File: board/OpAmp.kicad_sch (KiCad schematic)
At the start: 15 parts, among them U3 Opamp_Dual, U8 Opamp_Dual

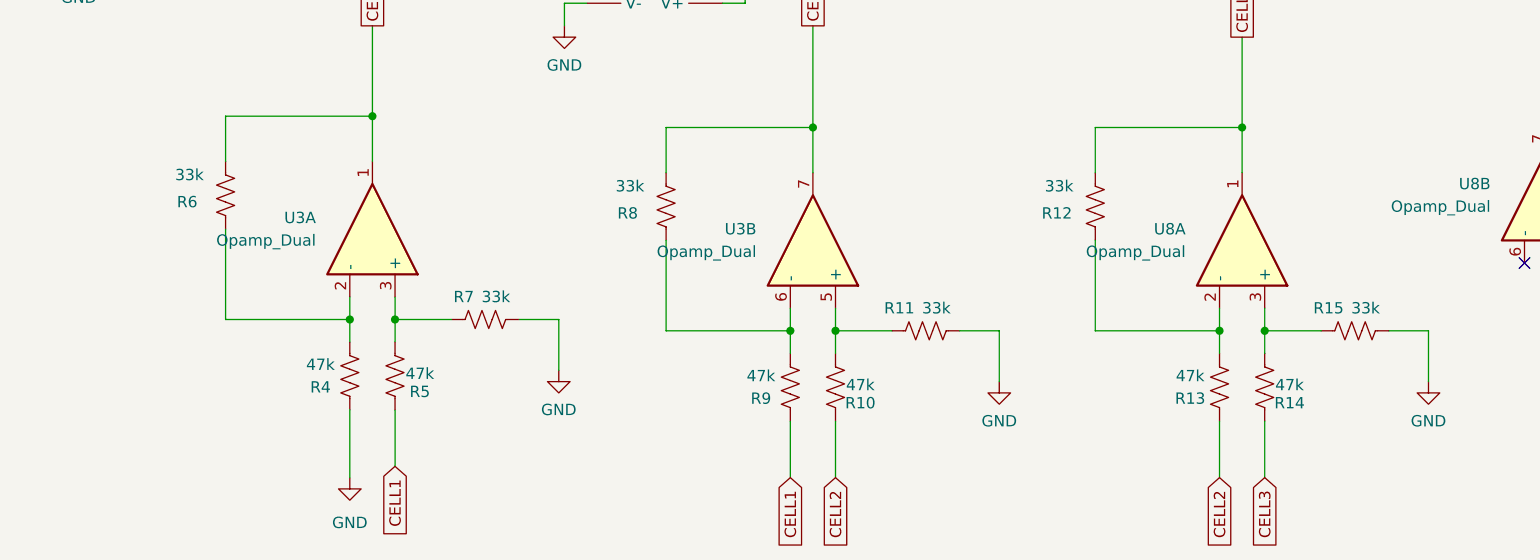
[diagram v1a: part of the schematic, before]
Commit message: Add Corrected Op-Amp Resistor Values
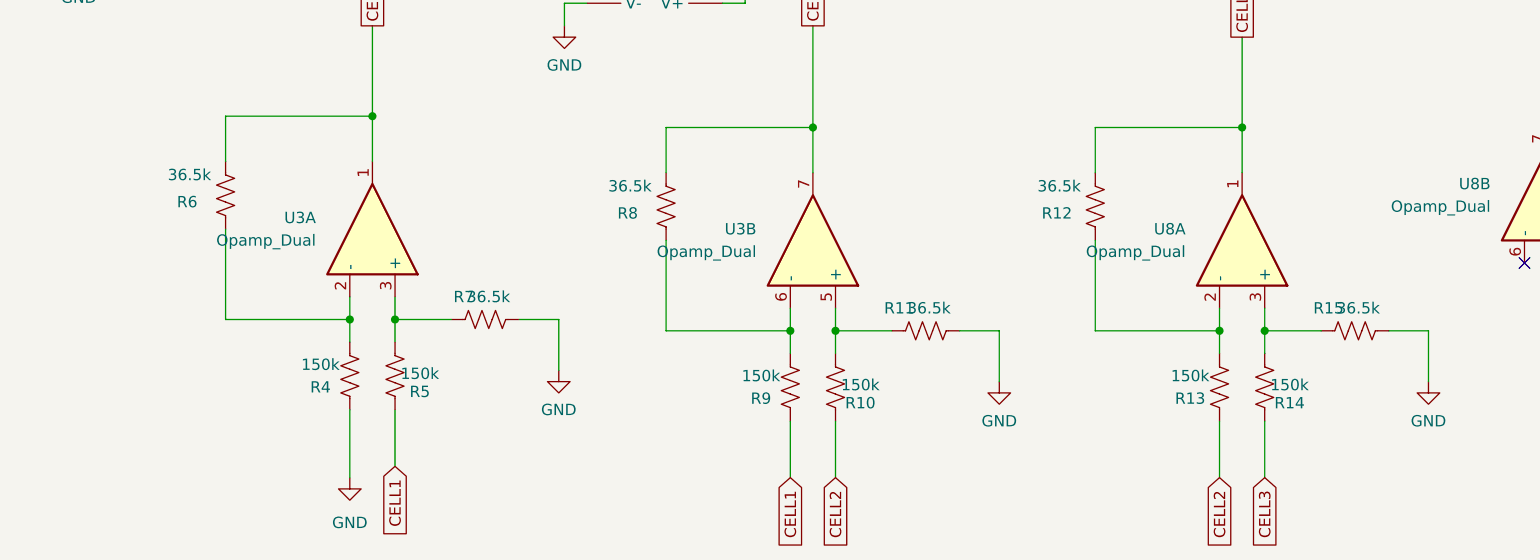
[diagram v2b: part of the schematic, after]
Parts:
- R10, R13, R14, R4, R5, R9: value 47k -> 150k
- R11, R12, R15, R6, R7, R8: value 33k -> 36.5k
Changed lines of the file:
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@@
 			)
 		)
-		(property "Value" "47k"
+		(property "Value" "150k"
 			(at 169.418 138.43 0)
 			(effects
@@
 			)
 		)
-		(property "Value" "47k"
+		(property "Value" "150k"
 			(at 119.888 137.16 0)
 			(effects
@@
 			)
 		)
-		(property "Value" "33k"
+		(property "Value" "36.5k"
 			(at 141.224 129.54 90)
 			(effects
@@
 			)
 		)
-		(property "Value" "47k"
+		(property "Value" "150k"
 			(at 131.064 138.176 0)
 			(effects
@@
 			)
 		)
-		(property "Value" "47k"
+		(property "Value" "150k"
 			(at 228.854 139.446 0)
 			(effects
@@
 			)
 		)
-		(property "Value" "33k"
+		(property "Value" "36.5k"
 			(at 239.014 130.81 90)
 			(effects
@@
 			)
 		)
-		(property "Value" "33k"
+		(property "Value" "36.5k"
 			(at 105.156 115.824 0)
 			(effects
@@
 			)
 		)
-		(property "Value" "47k"
+		(property "Value" "150k"
 			(at 180.594 139.446 0)
 			(effects
@@
 			)
 		)
-		(property "Value" "47k"
+		(property "Value" "150k"
 			(at 217.678 138.43 0)
 			(effects
@@
 			)
 		)
-		(property "Value" "33k"
+		(property "Value" "36.5k"
 			(at 202.946 117.094 0)
 			(effects
@@
 			)
 		)
-		(property "Value" "33k"
+		(property "Value" "36.5k"
 			(at 154.686 117.094 0)
 			(effects
@@
 			)
 		)
-		(property "Value" "33k"
+		(property "Value" "36.5k"
 			(at 190.754 130.81 90)
 			(effects
